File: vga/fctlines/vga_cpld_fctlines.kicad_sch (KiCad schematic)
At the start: 9 parts, among them U15 74HC157, U16 74HC157, U17 ATF1508AS-xJx84, U20 ATF1502AS-xJx44, U24 AT28C16, U25 74HC541, Y1 CXO_DIP8_25.175MHz

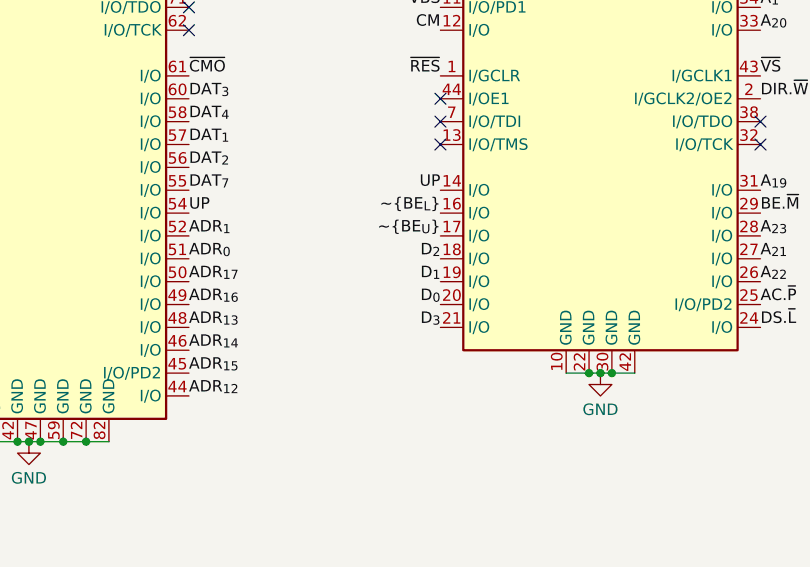
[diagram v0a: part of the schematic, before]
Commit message: [vga/fctlines] corrected errors on schematic. Schematic & PCB are NO longer matching.
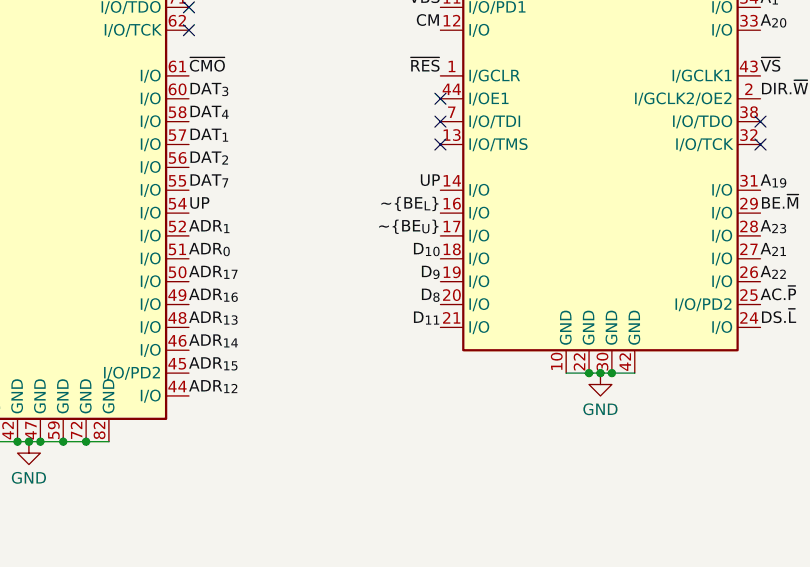
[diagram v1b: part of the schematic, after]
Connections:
- net D_{0} renamed D_{8}
- net D_{1} renamed D_{9}
- net D_{2} renamed D_{10}
- net D_{3} renamed D_{11}
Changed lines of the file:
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@@
 		)
 	)
-	(label "D_{1}"
+	(label "D_{9}"
 		(at 147.32 107.95 180)
 		(effects
@@
 		)
 	)
-	(label "D_{2}"
+	(label "D_{10}"
 		(at 147.32 105.41 180)
 		(effects
@@
 		)
 	)
-	(label "D_{0}"
+	(label "D_{8}"
 		(at 147.32 110.49 180)
 		(effects
@@
 		)
 	)
-	(label "D_{3}"
+	(label "D_{11}"
 		(at 147.32 113.03 180)
 		(effects
